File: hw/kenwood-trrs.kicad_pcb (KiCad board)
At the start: 2 copper layers, 11.8 x 27.8 mm, 12 parts, among them J1 TRRS Jack, J2 BAOFENG2.5SPK, J3 BAOFENG3.5MIC, Q1 BSS138, Q2 BSS83P

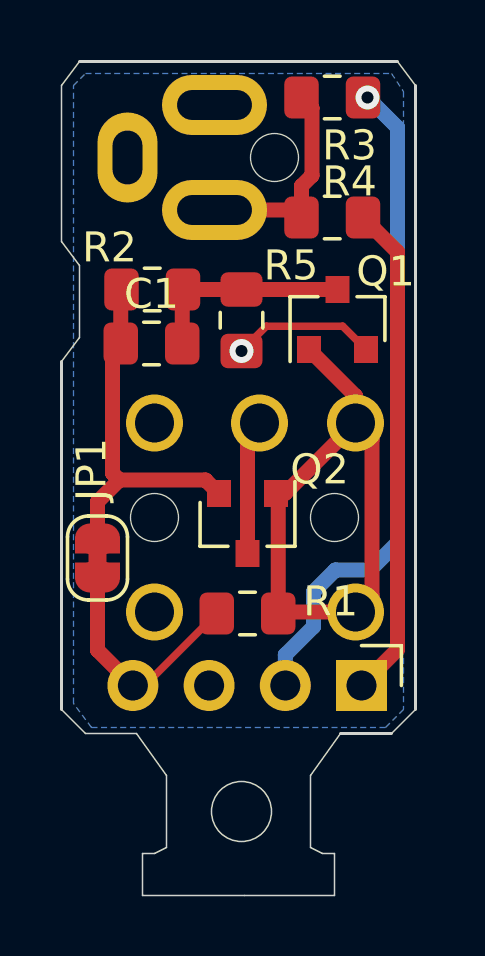
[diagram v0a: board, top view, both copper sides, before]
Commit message: fixed jack footprints
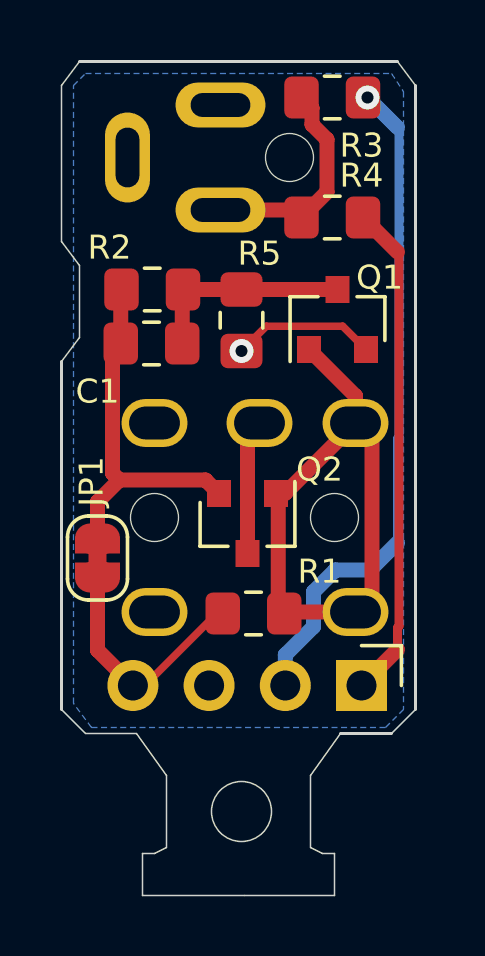
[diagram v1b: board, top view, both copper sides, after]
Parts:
- moved R1 0.20 mm to (154.4, 92.0)

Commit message: new version with different muting mechanism
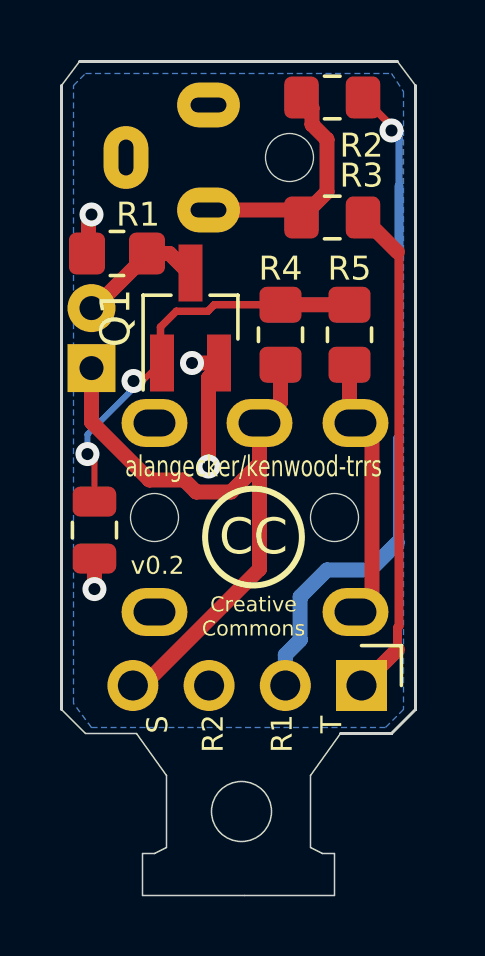
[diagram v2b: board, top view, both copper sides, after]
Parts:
- removed JP1: Jumper_NC_Small, Jumper:SolderJumper-2_P1.3mm_Bridged_RoundedPad1.0x1.5mm
- removed Q2: BSS83P, Package_TO_SOT_SMD:SOT-23
- removed the R2 at (151.0, 81.2)
- added C2: NC, Capacitor_SMD:C_0805_2012Metric, F.Cu at (149.1, 89.2)
- added R4: 2M, Resistor_SMD:R_0805_2012Metric_Pad1.20x1.40mm_HandSolder, F.Cu at (155.3, 82.7)
- C1: value C_Small -> 100u 6.3V; footprint Capacitor_SMD:C_0805_2012Metric_Pad1.15x1.40mm_HandSolder -> Capacitor_THT:CP_Radial_D5.0mm_P2.00mm; moved to B.Cu
- Q1: value BSS138 -> AO3400A; footprint Package_TO_SOT_SMD:SOT-23 -> Package_TO_SOT_SMD:SOT-23_Handsoldering
- R1: value 47k -> 100k; footprint Resistor_SMD:R_0805_2012Metric_Pad1.15x1.40mm_HandSolder -> Resistor_SMD:R_0805_2012Metric_Pad1.20x1.40mm_HandSolder
- R5: value R_Small -> 100K; footprint Resistor_SMD:R_0805_2012Metric_Pad1.15x1.40mm_HandSolder -> Resistor_SMD:R_0805_2012Metric_Pad1.20x1.40mm_HandSolder
- moved R1 12.8 mm to (149.8, 80.0), turned to 180 degrees
- moved Q1 4.90 mm to (152.3, 82.2)
- moved R5 3.63 mm to (157.6, 82.7), turned to 90 degrees
- moved C1 2.16 mm to (149.0, 83.8), turned to 90 degrees
- renumbered R3 to R2, R4 to R3
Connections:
- C1 pad 1: /Mic' -> /Mic+
- C1 pad 2: /N-FET_D -> Net-(C1-Pad2)
- J1 pad S: /Mic -> /Mic+
- J2 pad R: Net-(J2-PadR) -> GND
- Q1 pad 1: /PTT_Mic- -> Net-(C2-Pad1)
- Q1 pad 3: /N-FET_D -> Net-(C1-Pad2)
- R1 pad 1: /Mic -> Net-(C1-Pad2)
- R1 pad 2: /PTT_Mic- -> GND
- R5 pad 1: /N-FET_D -> /PTT_Mic-
- R5 pad 2: GND -> Net-(C2-Pad1)
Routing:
- net /Mic+: track 4.52 -> 22.0 mm
- net Net-(C2-Pad1): track 0.00 -> 13.7 mm, vias 0 -> 2
- net /Mic': track 12.3 -> 0.00 mm
- net /PTT_Mic-: track 20.1 -> 8.78 mm
- net /Mic: track 8.22 -> 0.00 mm
- net /N-FET_D: track 6.96 -> 0.00 mm
- net Net-(C1-Pad2): track 0.00 -> 4.27 mm
- net GND: track 4.81 -> 6.56 mm, vias 1 -> 4
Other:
- outline, holes or cut-outs redrawn
- board text added: "R1"
- board text added: "R2"
- board text added: "S"
- board text added: "T"
- board text added: "v0.2"
- board text removed: "v0.1"
